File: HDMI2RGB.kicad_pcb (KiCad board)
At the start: 4 copper layers, 58.4 x 63.5 mm, 114 parts, among them J1 HDMI_A, J2 QTH-030-02-L-DA, J3 RAPC712x, P1 CONN_02X07, P2 CONN_01X06, P3 CONN_01X06, SW1 2M1-SP1-T2-B4-M6RE, U1 TPD4S010DQAR, U10 TPS62260, U11 TPS62260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

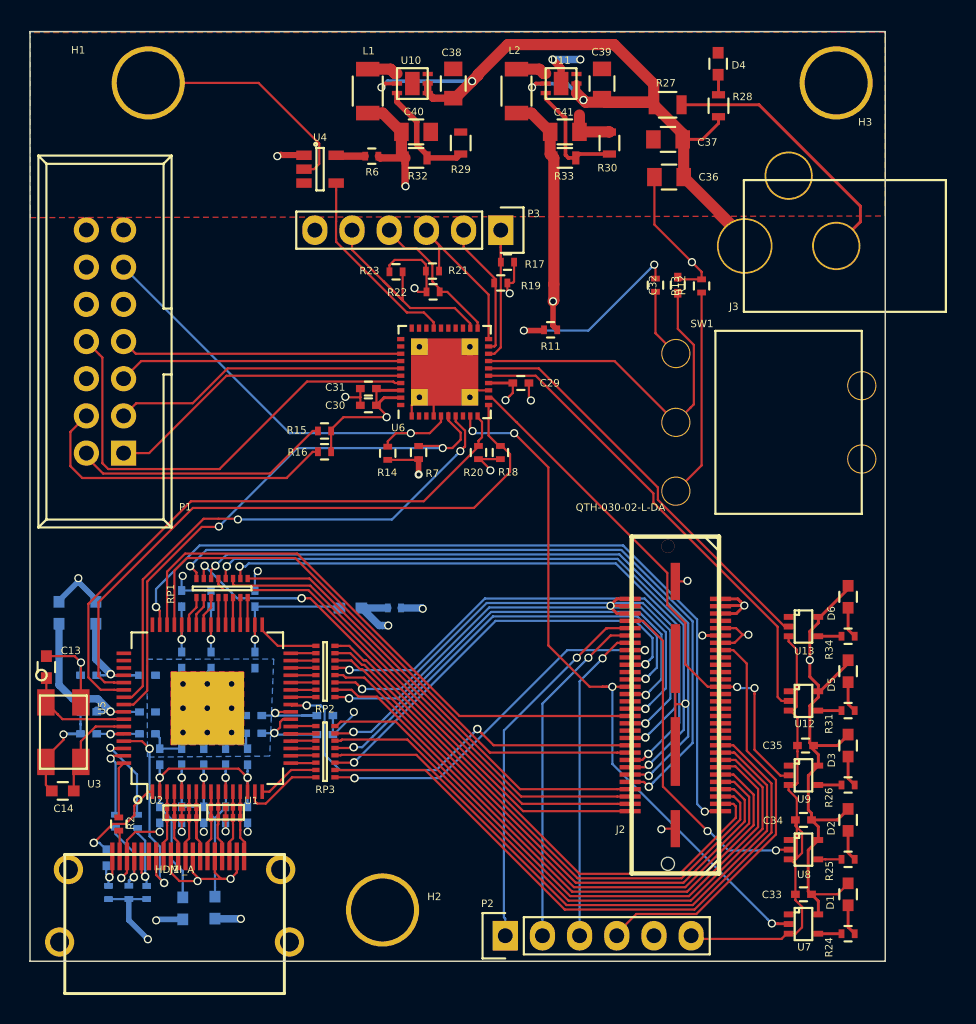
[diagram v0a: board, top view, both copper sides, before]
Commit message: Added silkscreen labels and title to PCB
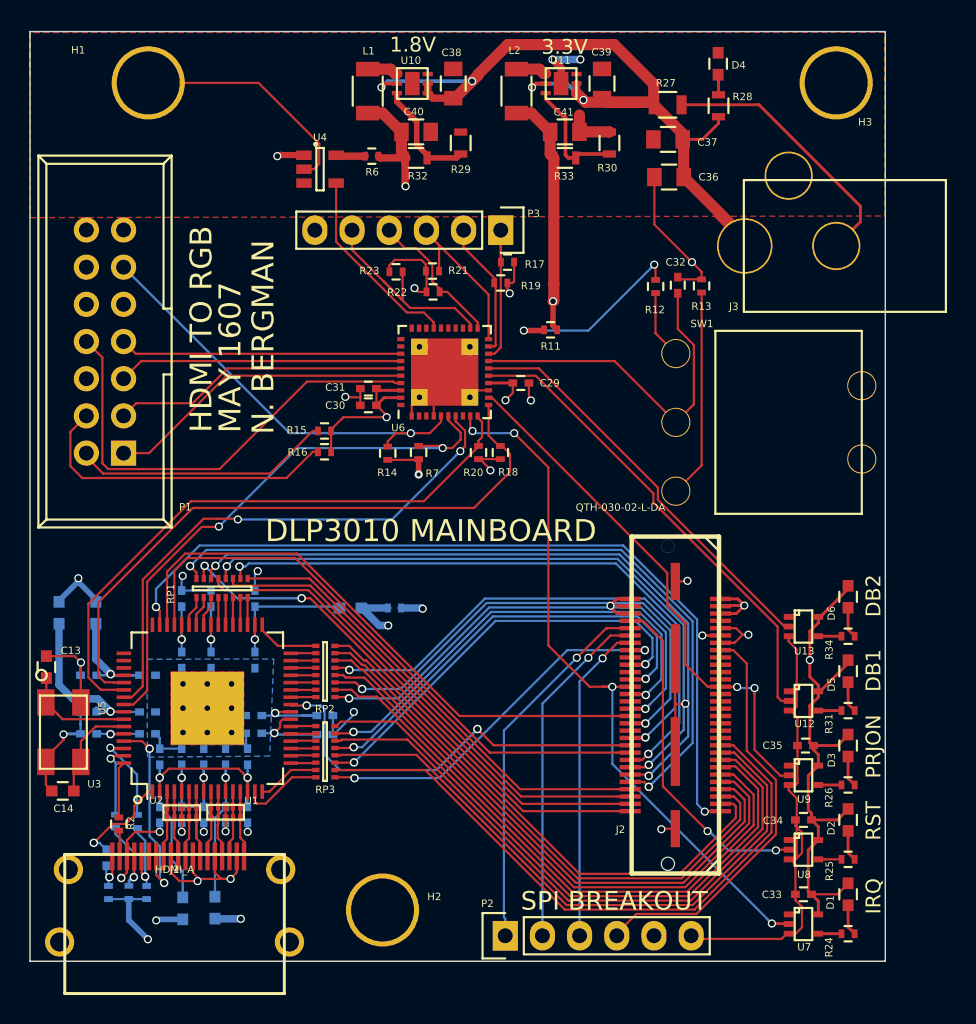
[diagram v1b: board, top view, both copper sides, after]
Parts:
- moved R12 0.09 mm to (88.5, 80.9)
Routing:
- net +3V3: track 187.7 -> 186.3 mm
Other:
- board text added: "1.8V"
- board text added: "3.3V"
- board text added: "DB1"
- board text added: "DB2"
- board text added: "DLP3010 MAINBOARD"
- board text added: "HDMI TO RGB"
- board text added: "IRQ"
- board text added: "MAY 1607"
- board text added: "N. BERGMAN"
- board text added: "PRJON"
- board text added: "RST"
- board text added: "SPI BREAKOUT"

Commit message: Changed via size to 23mil diameter
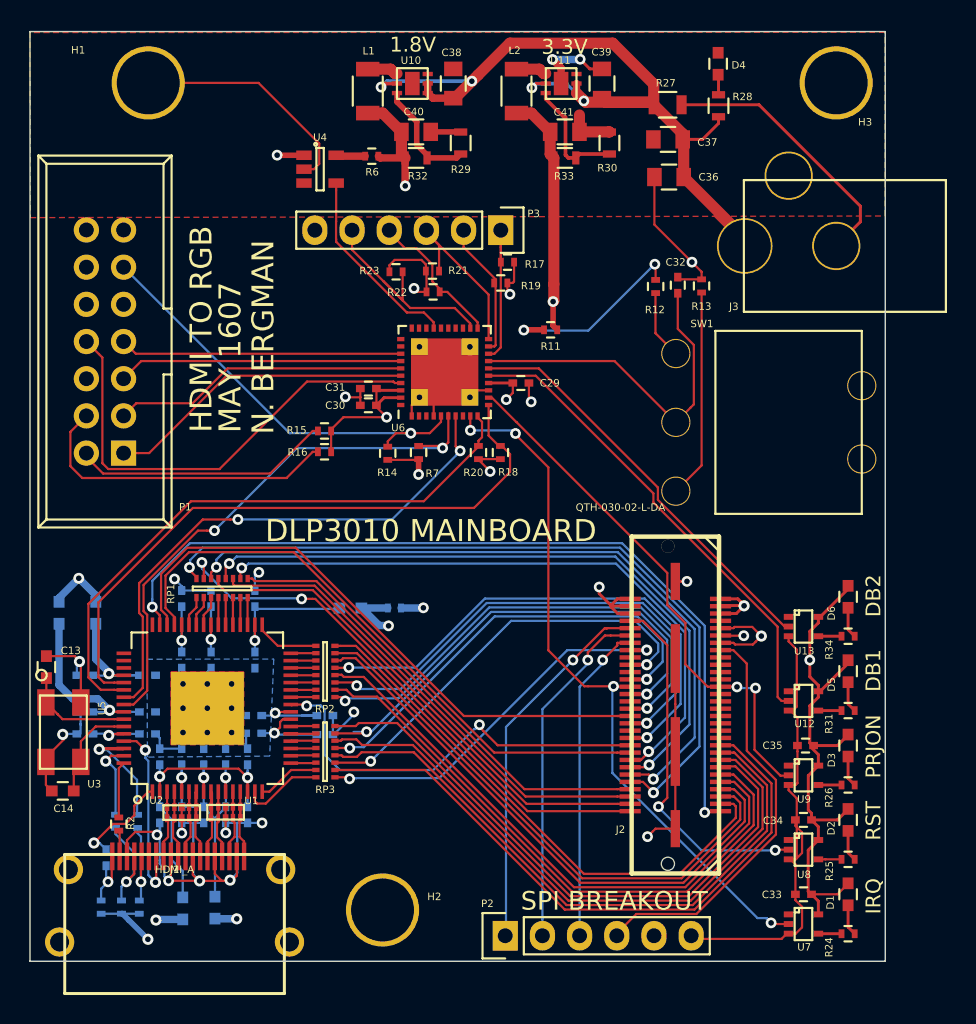
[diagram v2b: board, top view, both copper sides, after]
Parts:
- moved R3 1.12 mm to (53.2, 123.3)
- moved R4 1.12 mm to (52.0, 123.3)
- moved R5 1.12 mm to (50.6, 123.3)
- moved C16 0.25 mm to (49.5, 111.5)
- moved C17 0.25 mm to (49.5, 110.0)
- moved C19 0.25 mm to (49.5, 107.5)
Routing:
- net GND: track 274.9 -> 298.1 mm, vias 21 -> 19
- net Net-(R9-Pad1): track 6.23 -> 9.23 mm
- net SYSPWR: track 105.4 -> 108.4 mm
- net +3V3: track 186.3 -> 188.8 mm
- net +1V8: track 67.8 -> 69.8 mm
- net /HDMI_INPUT/HDMI_CLK_N: track 6.84 -> 4.85 mm
- net /CONNECTOR/RESETZ: track 23.2 -> 24.7 mm
- net /HDMI_INPUT/HDMI_HPA: track 3.00 -> 4.51 mm
- net /CONNECTOR/PDATA0: track 51.8 -> 53.3 mm
- net /HDMI_INPUT/ADV_VDD1V8: track 74.4 -> 72.9 mm
- net /HDMI_INPUT/HDMI_CLK_P: track 5.99 -> 4.65 mm
- net /CONNECTOR/PDATA23: track 25.8 -> 27.1 mm
- net /CONNECTOR/PDATA17: track 32.1 -> 33.3 mm
- net /HDMI_INPUT/HDMI_SDA: track 6.53 -> 7.79 mm
- net /CONNECTOR/PDATA2: track 48.4 -> 49.6 mm
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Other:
- net class Default: via_dia 0.5588 -> 0.7366
- net class POWER_IN: via_dia 0.5588 -> 0.7366
- rule trace_min: 0.006 -> 0.1524
- rule via_min_size: 0.022 -> 0.7366
